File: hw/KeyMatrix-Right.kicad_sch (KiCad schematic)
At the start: 135 parts, among them SW1500 SW_Cherry_MX_RGB, SW1501 SW_Cherry_MX_RGB, SW1502 SW_Cherry_MX_RGB, SW1503 SW_Cherry_MX_RGB, SW1504 SW_Cherry_MX_RGB, SW1505 SW_Cherry_MX_RGB, SW1506 SW_Cherry_MX_RGB, SW1507 SW_Cherry_MX_RGB, SW1508 SW_Cherry_MX_RGB, SW1509 SW_Cherry_MX_RGB, SW1510 SW_Cherry_MX_RGB, SW1511 SW_Cherry_MX_RGB, SW1512 SW_Cherry_MX_RGB, SW1513 SW_Cherry_MX_RGB, SW1514 SW_Cherry_MX_RGB, SW1515 SW_Cherry_MX_RGB, SW1516 SW_Cherry_MX_RGB, SW1517 SW_Cherry_MX_RGB, SW1518 SW_Cherry_MX_RGB, SW1519 SW_Cherry_MX_RGB, SW1520 SW_Cherry_MX_RGB, SW1521 SW_Cherry_MX_RGB, SW1522 SW_Cherry_MX_RGB, SW1523 SW_Cherry_MX_RGB, SW1524 SW_Cherry_MX_RGB, SW1525 SW_Cherry_MX_RGB, SW1526 SW_Cherry_MX_RGB, SW1527 SW_Cherry_MX_RGB, SW1528 SW_Cherry_MX_RGB, SW1529 SW_Cherry_MX_RGB, SW1530 SW_Cherry_MX_RGB, SW1531 SW_Cherry_MX_RGB, SW1532 SW_Cherry_MX_RGB, SW1533 SW_Cherry_MX_RGB, SW1534 SW_Cherry_MX_RGB, SW1535 SW_Cherry_MX_RGB, SW1536 SW_Cherry_MX_RGB, SW1537 SW_Cherry_MX_RGB, SW1538 SW_Cherry_MX_RGB, SW1539 SW_Cherry_MX_RGB, SW1540 SW_Cherry_MX_RGB, SW1541 SW_Cherry_MX_RGB, X1500 Keycap-R1-1x1, X1501 Keycap-R1-1x1, X1502 Keycap-R1-1x1, X1503 Keycap-R1-1x1, X1504 Keycap-R1-1x1, X1505 Keycap-R1-1x1, X1506 Keycap-R1-1x1, X1507 Keycap-R1-1x1, X1508 Keycap-R1-1x1, X1509 Keycap-R1-1x1, X1510 Keycap-R1-1x1, X1511 Keycap-R1-1x1, X1512 Keycap-R1-1x1, X1513 Keycap-R1-1x1, X1514 Keycap-R1-1x1, X1515 Keycap-R1-1x1, X1516 Keycap-R1-1x1, X1517 Keycap-R1-1x1, X1518 Keycap-R1-1x1, X1519 Keycap-R1-1.5x1, X1520 Keycap-R1-1x1, X1521 Keycap-R1-1x1, X1522 Keycap-R1-1x1, X1523 Keycap-R1-1x1, X1524 Keycap-R1-1x1, X1525 Keycap-R1-1x1, X1526 Keycap-R1-1.75x1, X1527 Keycap-R1-2x1, X1528 Keycap-R1-1x1, X1529 Keycap-R1-1x1, X1530 Keycap-R1-1x1, X1531 Keycap-R1-1x1, X1532 Keycap-R1-1x1, X1533 Keycap-R1-1x1, X1534 Keycap-R1-1.25x1, X1535 Keycap-R1-2x1, X1536 Keycap-R1-1.25x1, X1537 Keycap-R1-1.25x1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

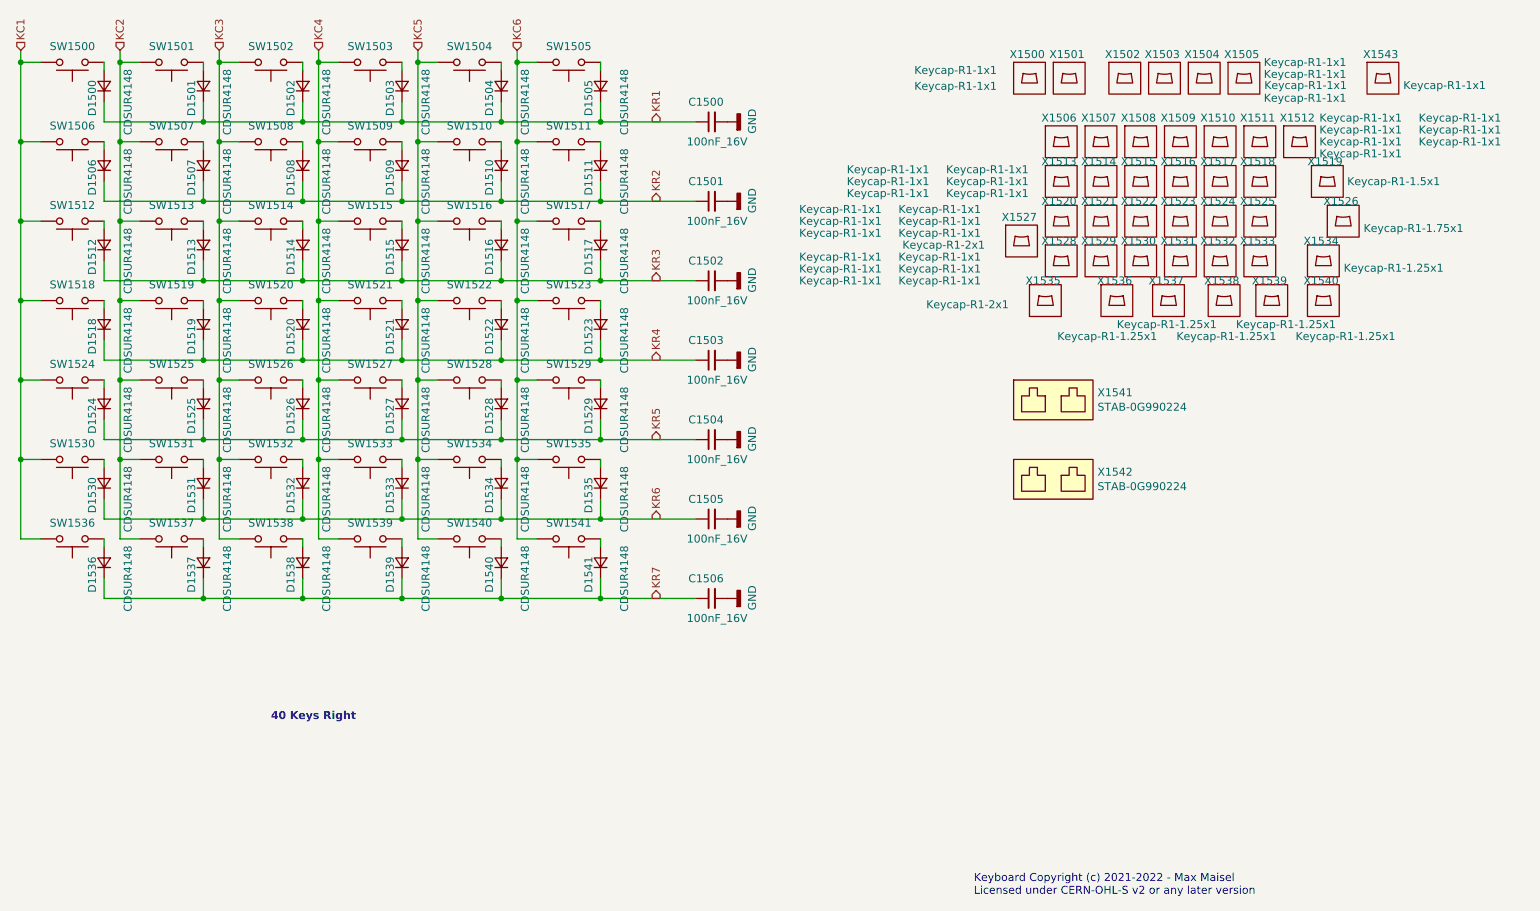
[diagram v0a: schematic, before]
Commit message: Add ESD diodes to key matrix pins.
Better save than sorry.
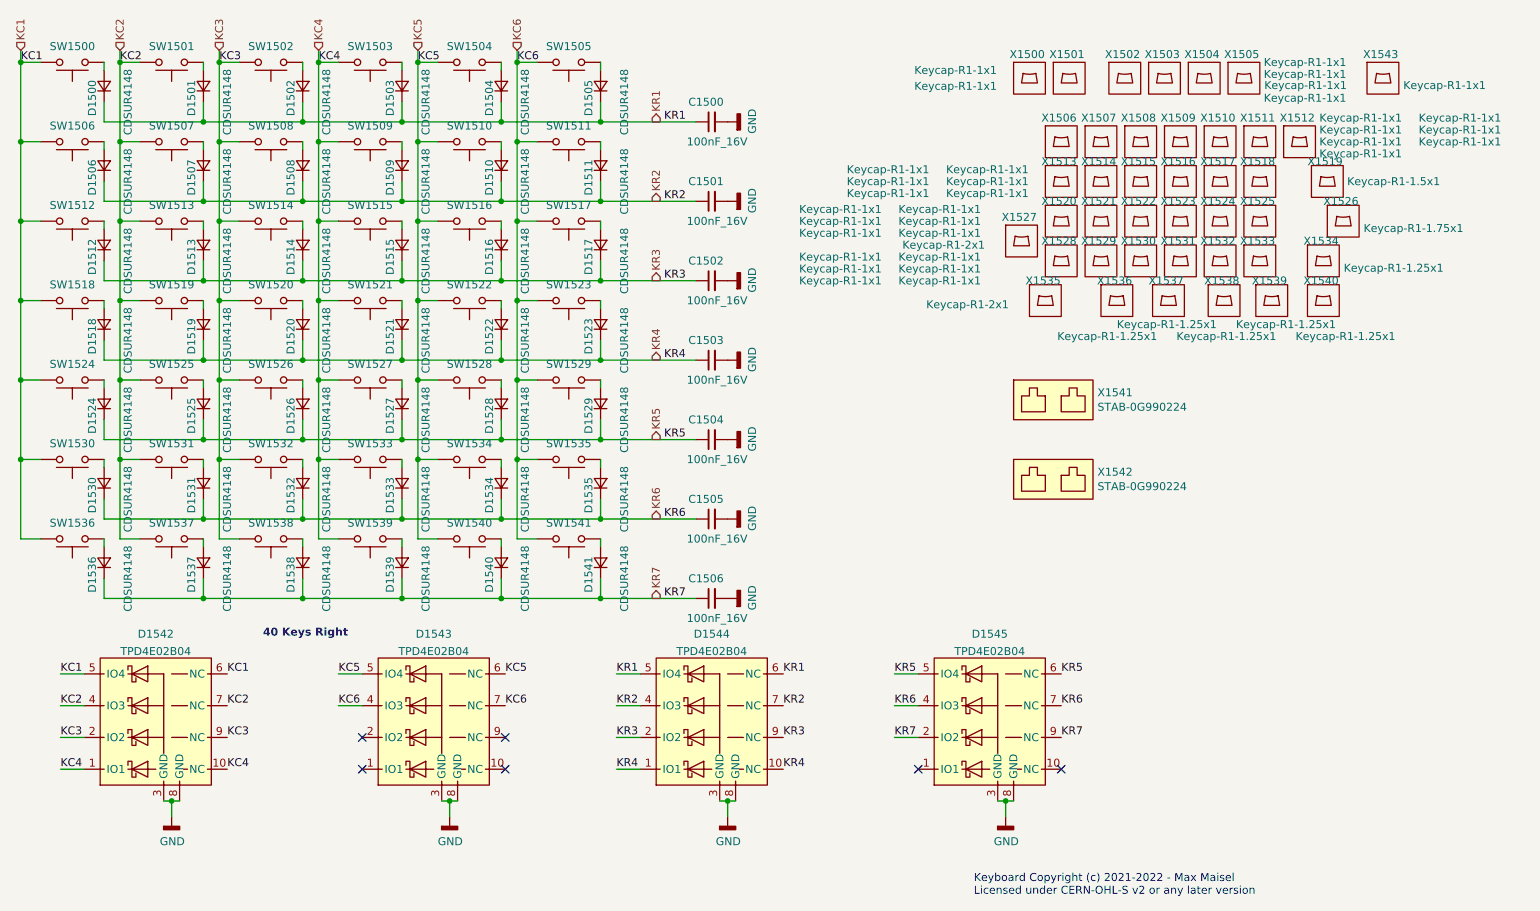
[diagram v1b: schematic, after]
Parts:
- added D1542, D1543, D1544, D1545: TPD4E02B04, Keyboard:USON10, symbol Keyboard:TPD4E02B04
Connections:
- net GND: now also D1542.3 (GND), D1542.8 (GND), D1543.3 (GND), D1543.8 (GND), D1544.3 (GND), D1544.8 (GND), D1545.3 (GND), D1545.8 (GND)
- net KC1: now also D1542.5 (IO4), D1542.6 (NC)
- net KC2: now also D1542.4 (IO3), D1542.7 (NC)
- net KC3: now also D1542.2 (IO2), D1542.9 (NC)
- net KC4: now also D1542.1 (IO1), D1542.10 (NC)
- net KC5: now also D1543.5 (IO4), D1543.6 (NC)
- net KC6: now also D1543.4 (IO3), D1543.7 (NC)
- net KR1: now also D1544.5 (IO4), D1544.6 (NC)
- net KR2: now also D1544.4 (IO3), D1544.7 (NC)
- net KR3: now also D1544.2 (IO2), D1544.9 (NC)
- net KR4: now also D1544.1 (IO1), D1544.10 (NC)
- net KR5: now also D1545.5 (IO4), D1545.6 (NC)
- net KR6: now also D1545.4 (IO3), D1545.7 (NC)
- net KR7: now also D1545.2 (IO2), D1545.9 (NC)
- no-connect marks 0 -> 6

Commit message: Update schematic:
- Add ESD protection.
- Adjust distance bolts so they fit to the MX mounting plate.
- Make key layout symmetric.
- Add resistor to TX driver outputs.
- Use alternate IO functions on inter-board connectors.
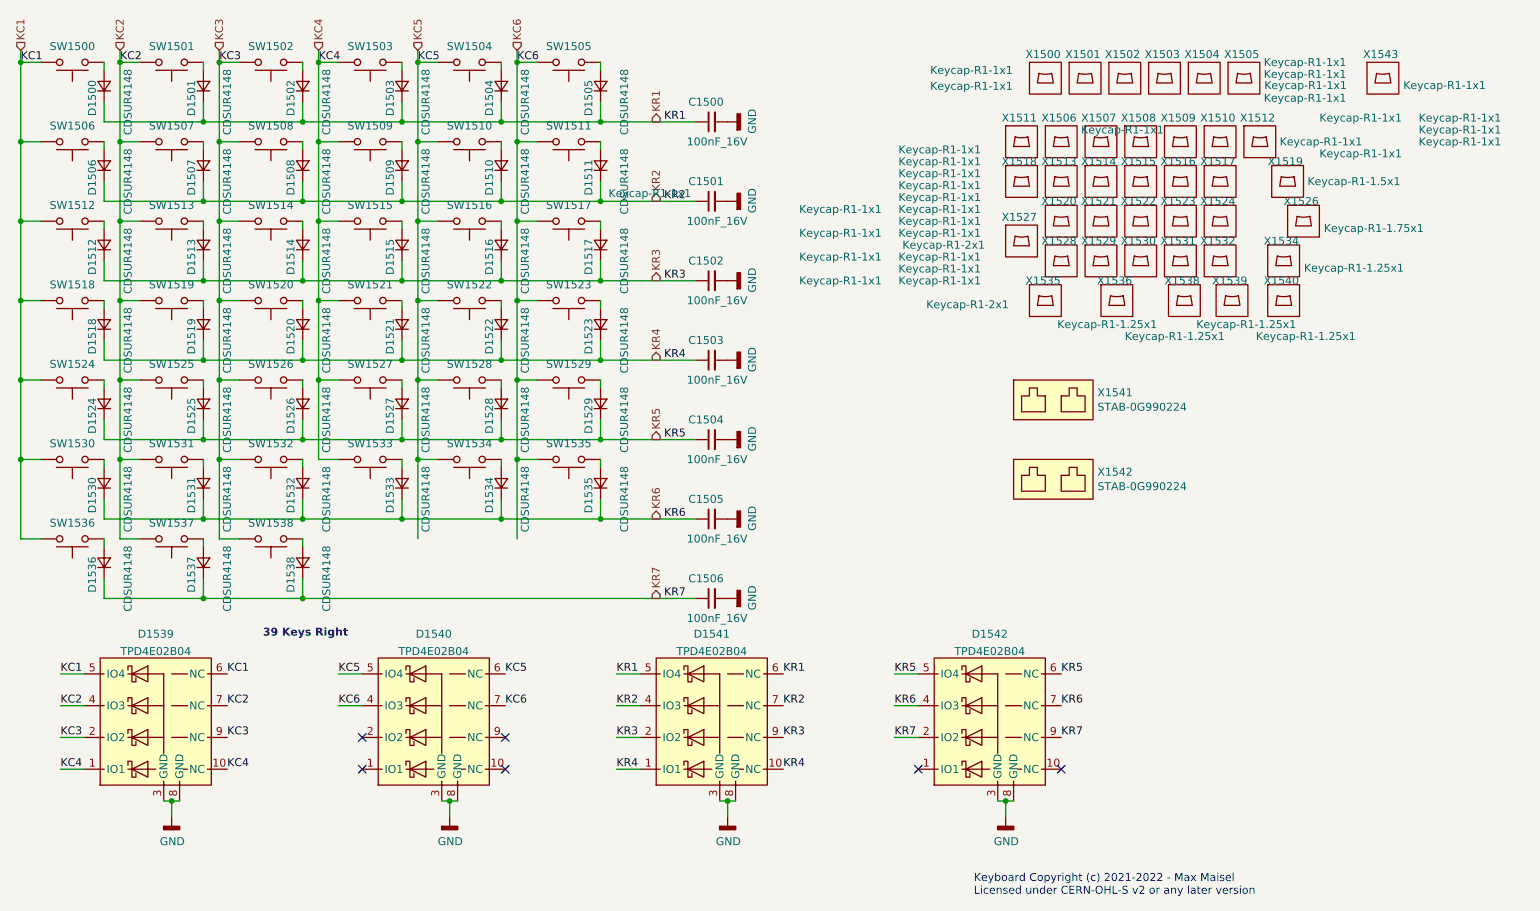
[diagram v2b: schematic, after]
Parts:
- removed D1539, D1540, D1541: CDSUR4148, Keyboard:SOD-523, symbol Keyboard:CDSUR4148
- removed SW1539, SW1540, SW1541: SW_Cherry_MX_RGB, Keyboard:SW_Cherry_MX1A_RGB, symbol Keyboard:SW_Cherry_MX_RGB
- removed X1525, X1533: Keycap-R1-1x1, Keyboard:Keycap-R1-1x1, symbol Keyboard:Keycap-R1-1x1
- removed X1537: Keycap-R1-1.25x1, Keyboard:Keycap-R1-1.25x1, symbol Keyboard:Keycap-R1-1.25x1
- renumbered D1542 to D1539, D1543 to D1540, D1544 to D1541, D1545 to D1542
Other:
- note added: "39 Keys Right"
- note removed: "40 Keys Right"
- moved on the sheet: X1500, X1501, X1511, X1512, X1518, X1519, X1526, X1534, X1538, X1539, X1540

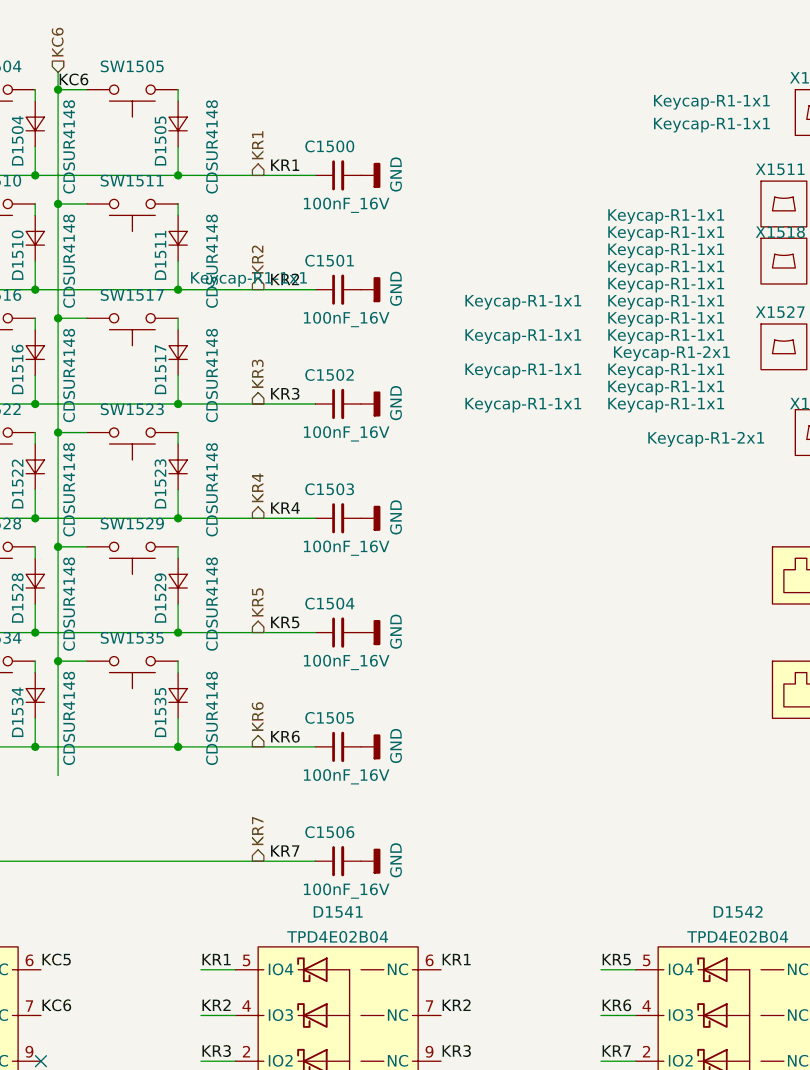
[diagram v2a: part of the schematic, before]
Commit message: Change key matrix capacitors to 220pF.
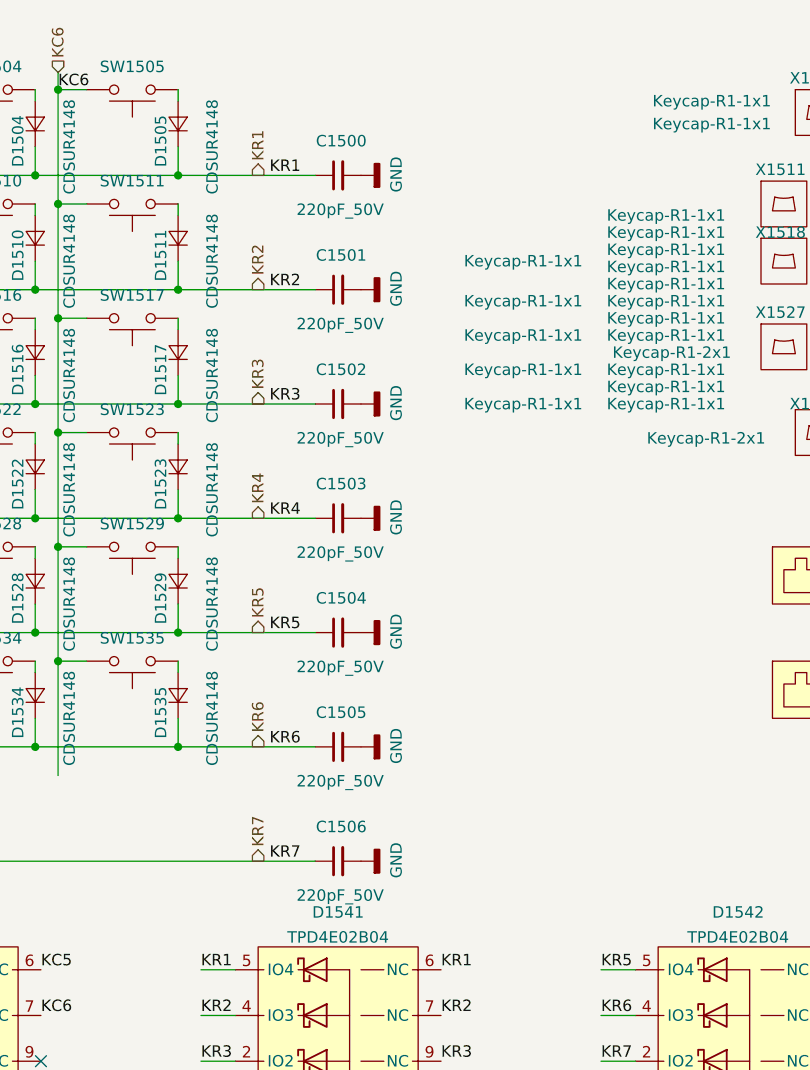
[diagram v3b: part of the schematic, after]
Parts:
- removed C1500, C1501, C1502, C1503, C1504, C1505, C1506: 100nF_16V, Keyboard:C_0402, symbol Keyboard:100nF_16V
- added C1500, C1501, C1502, C1503, C1504, C1505, C1506: 220pF_50V, Keyboard:C_0402, symbol Keyboard:220pF_50V
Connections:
- net GND: now also C1500.2, C1501.2, C1502.2, C1503.2, C1504.2, C1505.2, C1506.2
- net KR1: now also C1500.1
- net KR2: now also C1501.1
- net KR3: now also C1502.1
- net KR4: now also C1503.1
- net KR5: now also C1504.1
- net KR6: now also C1505.1
- net KR7: now also C1506.1
